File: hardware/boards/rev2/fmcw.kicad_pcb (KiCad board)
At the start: 4 copper layers, 118.6 x 83.2 mm, 445 parts, among them CON1 BARREL_JACK, J1 SD_Card, J2 USB_B_Micro, J3 SMA, J4 SMA, J5 SMA, J6 Conn_02x08_Odd_Even, Q1 DNP(RE1C002UN), Q2 RE1C002UN, SW1 SW_PUSH, T1 uwave, T10 uwave, T11 uwave, T12 uwave, T13 uwave, T14 uwave, T2 uwave, T3 uwave, T4 uwave, T5 uwave, T6 uwave, T7 uwave, T8 uwave, T9 uwave, U1 LP5907MFX-3.3, U10 LP5907MFX-3.0, U11 LTC2292, U12 ADF4158, U13 TLV172DCK, U14 PAT1220-C-3DB, U15 HMC431, U16 PD4859J5050S2HF, U17 PAT1220-C-5DB, U18 SE5004L, U2 LP5907MFX-1.8, U20 PAT1220-C-6DB, U21 LMV321, U22 TRF37A73, U23 SKY65404, U24 TRF37A73, U25 SKY65404, U26 L7980, U27 L7980, U28 L7980, U29 LP2985A-10DBVR, U3 KT2520K-T, U30 TPS7A91, U31 TPS7A91, U32 TPS7A91, U33 LP5907MFX-3.0, U34 TPS7A91, U35 5400BL15B050E, U36 5400BL15B050E, U37 5400BL15B050E, U38 ADL5802, U39 ADA4940-2, U4 NC7SVU04P5X, U40 TPS7A91, U5 NB3N551, U6 XC7A15T-FTG256, U7 W25Q32JV, U8 93LCxxBxxOT, U9 FT2232H, Y1 12MHz

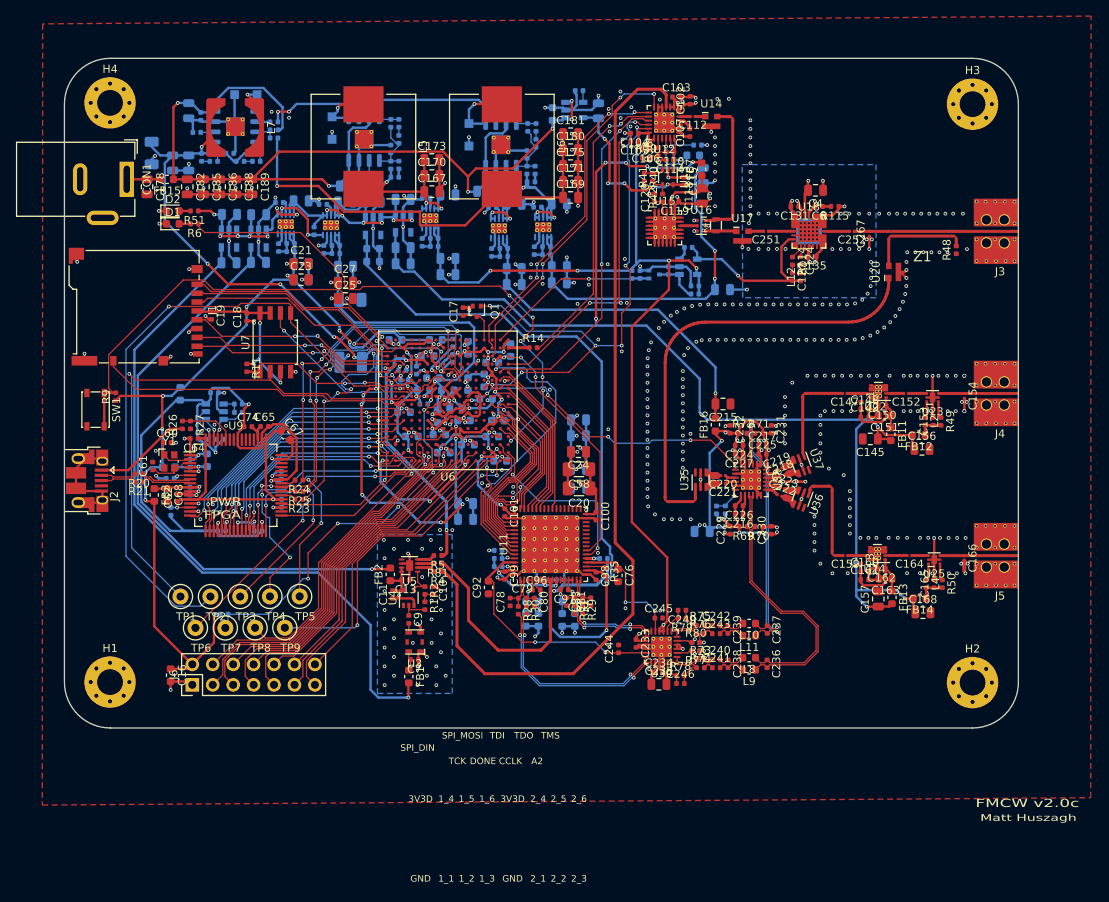
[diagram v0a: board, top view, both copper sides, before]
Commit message: switch ftclk to MRCC pin and place silkscreen
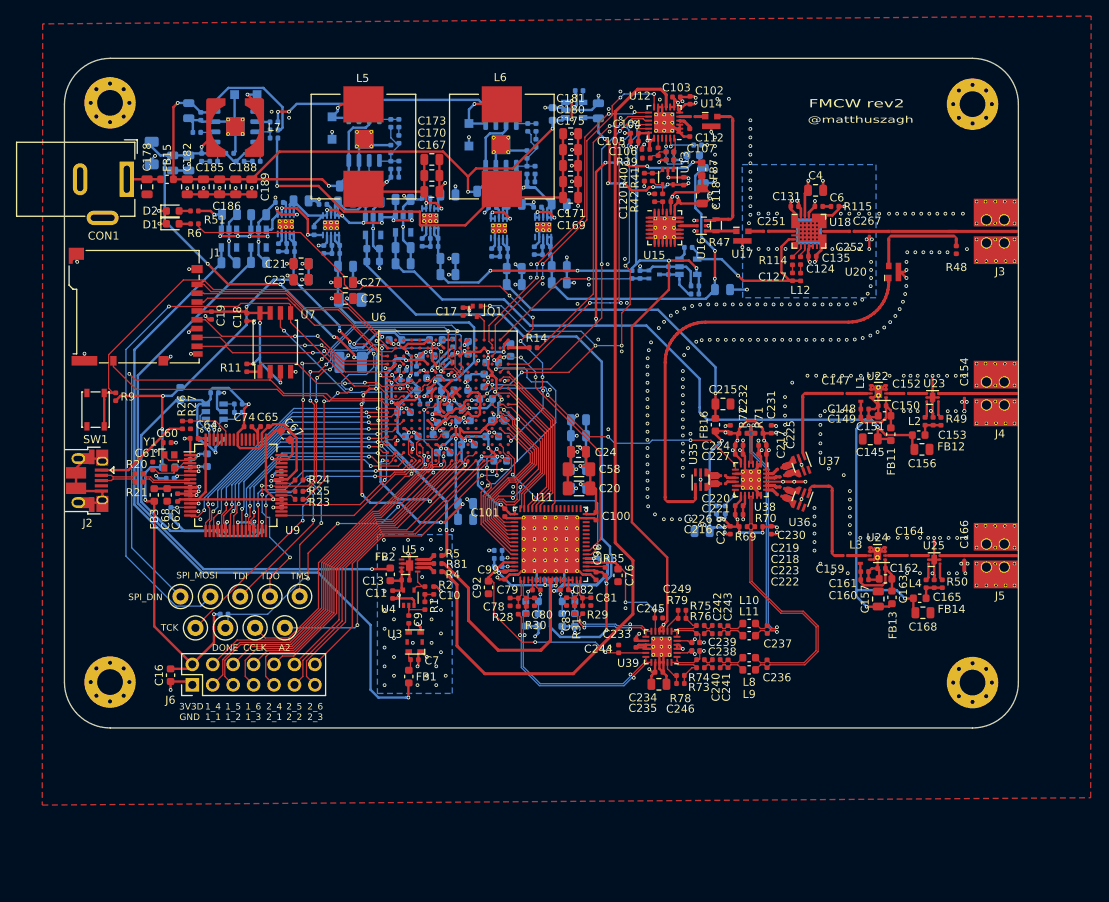
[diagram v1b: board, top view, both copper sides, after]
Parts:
- U22, U24: footprint fmcw_v5:WSON-8-1EP_2x2mm_P0.5mm_EP0.9x1.6mm_ThermalVias -> Package_SON:WSON-8-1EP_2x2mm_P0.5mm_EP0.9x1.6mm_ThermalVias
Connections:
- U6 pad A15: /fpga/CLKOUT -> (no net)
- U6 pad D13: (no net) -> /fpga/CLKOUT
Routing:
- net GND: track 555.8 -> 561.4 mm
- net /fpga/CLKOUT: track 27.7 -> 28.4 mm
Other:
- board text added: "@matthuszagh"
- board text added: "FMCW rev2"
- board text removed: "FMCW v2.0c"
- board text removed: "FPGA"
- board text removed: "Matt Huszagh"
- board text removed: "PWR"
